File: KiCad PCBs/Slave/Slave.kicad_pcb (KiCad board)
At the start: 2 copper layers, 51 parts, among them J1 Screw_Terminal_01x02, J10 AVR-ISP-6, J11 Conn_01x06_Female, J12 Screw_Terminal_01x02, J13 Screw_Terminal_01x02, J14 Screw_Terminal_01x02, J15 Screw_Terminal_01x02, J16 Screw_Terminal_01x02, J2 Screw_Terminal_01x02, J3 Screw_Terminal_01x02, J4 Screw_Terminal_01x02, J5 Screw_Terminal_01x02, J6 Screw_Terminal_01x02, J7 Screw_Terminal_01x02, J8 Screw_Terminal_01x02, J9 Screw_Terminal_01x02, SW1 SW_DIP_x02, SW1 SW_DIP_x04, SW2 SW_DIP_x02, SW3 SW_MEC_5E, U1 ATmega328P-AU, U2 MAX487ESA+T, U3 ULN2003A, U4 LM358DR2G, U5 AMS1117-5.0, Y1 Crystal_GND24

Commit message: Slave PCB wip
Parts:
- removed the SW1 at (59.7, 137.7)
- moved C9 132.2 mm to (148.9, 110.5), turned to -45 degrees
- moved C8 123.1 mm to (147.0, 108.7), turned to -45 degrees
- moved Y1 104.6 mm to (145.9, 111.0), turned to -45 degrees
- moved C6 98.1 mm to (137.6, 99.7), turned to 180 degrees
- moved J11 91.7 mm to (121.3, 125.1)
- moved U3 75.6 mm to (121.3, 95.9), turned to 90 degrees
- moved RJ1 70.0 mm to (106.0, 110.5), turned to -90 degrees
- moved U2 47.7 mm to (140.8, 95.9), turned to 90 degrees
- moved J10 36.1 mm to (110.5, 128.9)
- moved U5 31.0 mm to (121.3, 108.6)
- moved U4 30.6 mm to (121.3, 116.8), turned to 90 degrees
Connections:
- C10 pad 1: VCC -> +12V
- U5 pad 3: VCC -> +12V
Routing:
- net +5V: track 11.6 -> 23.2 mm
- net TXD: track 0.00 -> 11.5 mm
- net XTAL1: track 0.00 -> 9.23 mm
- net XTAL2: track 0.00 -> 9.05 mm
- net D2: track 0.00 -> 6.79 mm, vias 0 -> 2
- net RXD: track 0.00 -> 5.72 mm

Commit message: Slave WIP
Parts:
- removed R5: 1K, Resistor_SMD:R_0402_1005Metric
- moved J7 151.2 mm to (162.9, 80.0), turned to -90 degrees
- moved D1 147.6 mm to (172.1, 118.1), turned to 90 degrees
- moved D2 146.0 mm to (165.1, 108.6)
- moved J8 130.1 mm to (152.9, 80.0), turned to -90 degrees
- moved R4 116.7 mm to (145.9, 88.3)
- moved SW3 113.9 mm to (165.1, 104.1)
- moved R2 112.4 mm to (167.6, 108.6), turned to 180 degrees
- moved J4 111.4 mm to (149.5, 128.3), turned to 90 degrees
- moved J9 110.0 mm to (142.9, 80.0), turned to -90 degrees
- moved C7 106.8 mm to (143.5, 94.0), turned to 90 degrees
- moved J16 100.7 mm to (130.8, 80.0), turned to -90 degrees
- moved J14 97.0 mm to (106.7, 80.0), turned to -90 degrees
- moved D5 96.1 mm to (145.4, 97.2)
- moved J5 95.7 mm to (159.5, 128.3), turned to 90 degrees
- moved J15 95.3 mm to (118.7, 80.0), turned to -90 degrees
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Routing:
- net +5V: track 23.2 -> 29.5 mm

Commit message: Slave WIP
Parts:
- removed D3, D4: D, A10 KiCad Libraries:SOD-123F_L2.8-W1.8-LS3.7-RD
- removed U4: LM358DR2G, Package_SO:SOIC-8_3.9x4.9mm_P1.27mm
- added R10: 1.8K, Resistor_SMD:R_0805_2012Metric, F.Cu at (121.3, 101.6)
- added R9: 1.8K, Resistor_SMD:R_0805_2012Metric, F.Cu at (121.3, 106.7)
- R7, R8: value 1K -> 1.8K; footprint Resistor_SMD:R_0402_1005Metric -> Resistor_SMD:R_0805_2012Metric
- moved C11 126.9 mm to (127.0, 87.6)
- moved C10 121.6 mm to (121.2, 96.5)
- moved R8 108.6 mm to (116.2, 87.0)
- moved R7 89.1 mm to (121.3, 104.1)
- moved J7 6.95 mm to (169.8, 80.0)
- moved J8 6.95 mm to (159.8, 80.0)
- moved J9 6.95 mm to (149.8, 80.0)
- moved U3 5.99 mm to (119.4, 115.6)
- moved SW1 0.90 mm to (130.8, 98.4)
- moved R6 0.81 mm to (127.6, 97.9)
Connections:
- R7 pad 2: +5V -> RXD
- R8 pad 2: ACT -> TXD
- RJ1 pad 1: +5V -> Net-(R9-Pad1)
- RJ1 pad 2: ACT -> Net-(R10-Pad1)
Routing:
- net +12V: track 0.00 -> 78.0 mm
- net RS485+: track 0.00 -> 35.3 mm
- net RS485-: track 0.00 -> 34.2 mm, vias 0 -> 2
- net +5V: track 29.5 -> 47.6 mm
- net Net-(R9-Pad1): track 0.00 -> 13.6 mm, vias 0 -> 2
- net Net-(R10-Pad1): track 0.00 -> 10.1 mm, vias 0 -> 2
- net RS485_GND: track 0.00 -> 8.71 mm
- net Net-(R6-Pad2): track 0.00 -> 5.71 mm
- net Net-(R7-Pad1): track 0.00 -> 5.49 mm
- net Net-(R8-Pad1): track 0.00 -> 4.70 mm
- net RXD: track 5.72 -> 8.26 mm
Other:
- board outline added: 83.8 x 71.1 mm
- board text added: "1 BCK LT"
- board text added: "1 RS485"
- board text added: "2 AUX LT"
- board text added: "2 TERM"

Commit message: Slave WIP
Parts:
- C8, C9: value 16pF -> 15pF
- R1, R2, R3, R4, R6: footprint Resistor_SMD:R_0402_1005Metric -> Resistor_SMD:R_0805_2012Metric
- moved J10 14.6 mm to (166.4, 105.4)
- moved R4 12.4 mm to (134.0, 91.4), turned to 180 degrees
- moved J13 12.1 mm to (105.4, 115.6)
- moved J12 11.4 mm to (105.4, 127.0)
- moved R2 10.0 mm to (164.6, 99.1), turned to 0 degrees
- moved SW3 9.86 mm to (167.6, 94.6)
- moved D2 9.86 mm to (167.6, 99.1), turned to 180 degrees
- moved J11 8.25 mm to (137.2, 91.4)
- moved SW2 4.66 mm to (134.6, 115.1)
- moved C7 1.91 mm to (145.4, 94.0), turned to 180 degrees
- moved C11 1.42 mm to (127.6, 86.4), turned to 90 degrees
- moved R8 1.35 mm to (115.3, 88.0), turned to 90 degrees
- moved R6 1.30 mm to (126.5, 97.3)
- moved D5 1.27 mm to (145.4, 95.9)
- moved U3 0.90 mm to (118.7, 114.9)
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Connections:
- J1 pad 1: D2 -> GND
- R1 pad 1: D13/SCK -> D13
- SW2 pad 1: D3 -> D5
- SW2 pad 2: D4 -> D6
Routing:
- net RESET: track 0.00 -> 55.5 mm, vias 0 -> 2
- net D13: track 0.00 -> 51.2 mm
- net TXD: track 11.5 -> 57.1 mm, vias 0 -> 6
- net D5: track 0.00 -> 43.1 mm
- net D6: track 0.00 -> 41.9 mm, vias 0 -> 2
- net D3: track 0.00 -> 38.4 mm, vias 0 -> 2
- net D12: track 0.00 -> 37.2 mm, vias 0 -> 2
- net D11: track 0.00 -> 36.8 mm, vias 0 -> 2
- net +5V: track 47.6 -> 83.8 mm, vias 0 -> 3
- net D4: track 0.00 -> 33.8 mm, vias 0 -> 2
- net D7: track 0.00 -> 32.7 mm
- net RXD: track 8.26 -> 40.6 mm, vias 0 -> 5
- net A0: track 0.00 -> 32.1 mm
- net A5: track 0.00 -> 31.0 mm
- net D8: track 0.00 -> 29.3 mm
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- added copper zone on F.Cu, net +5V
- added copper zone on B.Cu, net GND
- added copper zone on F.Cu, net GND
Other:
- board size 83.8 x 71.1 mm -> 73 x 55.9 mm
- board text added: "GND"
- board text added: "INPUT ← D5 → BACKLIGHT"
- board text added: "INPUT ← D6 → AUX LIGHT"
- board text added: "OFF ← RS485 → ON"
- board text added: "OFF ← TERM → ON"
- board text added: "WarthogAtHome.com"
- board text removed: "1 BCK LT"
- board text removed: "1 RS485"
- board text removed: "2 AUX LT"
- board text removed: "2 TERM"

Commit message: Generated Final Rev 1 files for Hub and Slave
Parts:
- removed R10, R9: 1.8K, Resistor_SMD:R_0805_2012Metric
- moved R8 17.2 mm to (121.3, 104.1), turned to 0 degrees
- moved R7 2.54 mm to (121.3, 101.6)
- moved J10 0.89 mm to (165.5, 105.4)
- moved R2 0.25 mm to (164.3, 99.1)
- moved U5 0.25 mm to (123.8, 91.8)
- moved R1 0.25 mm to (172.1, 114.8)
- moved SW2 0.13 mm to (134.5, 115.1)
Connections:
- RJ1 pad 1: Net-(R9-Pad1) -> TXD
- RJ1 pad 2: Net-(R10-Pad1) -> RXD
- SW3 pad 1: unconnected-(SW3-Pad1) -> GND
- SW3 pad 4: unconnected-(SW3-Pad4) -> RESET
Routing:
- net Net-(R8-Pad1): track 2.77 -> 16.5 mm, vias 0 -> 2
- net Net-(R9-Pad1): track 13.6 -> 0.00 mm, vias 2 -> 0
- net RXD: track 40.6 -> 52.6 mm, vias 5 -> 6
- net Net-(R10-Pad1): track 10.1 -> 0.00 mm, vias 2 -> 0
- net RESET: track 55.5 -> 57.8 mm
- net TXD: track 57.1 -> 55.7 mm
- net D12: track 37.2 -> 36.3 mm
- net D11: track 36.8 -> 35.9 mm
- net +5V: track 83.8 -> 83.1 mm
- net D13: track 51.2 -> 50.6 mm
- net GND: track 7.11 -> 7.21 mm, vias 33 -> 38
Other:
- board text added: "BRRRRRRRRT"
- board text removed: "GND"

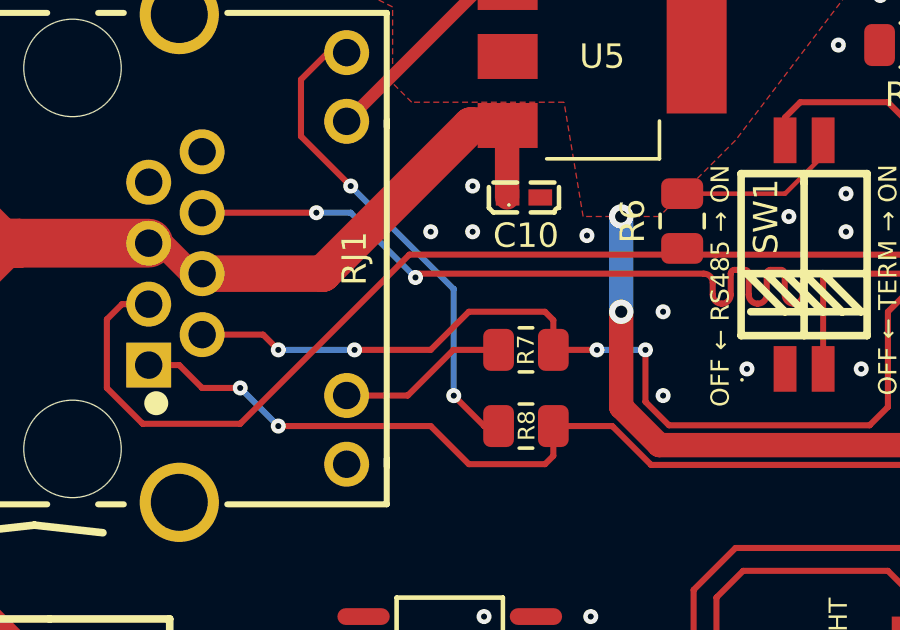
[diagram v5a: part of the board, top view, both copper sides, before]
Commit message: Fixed swapped LEDs on Slave
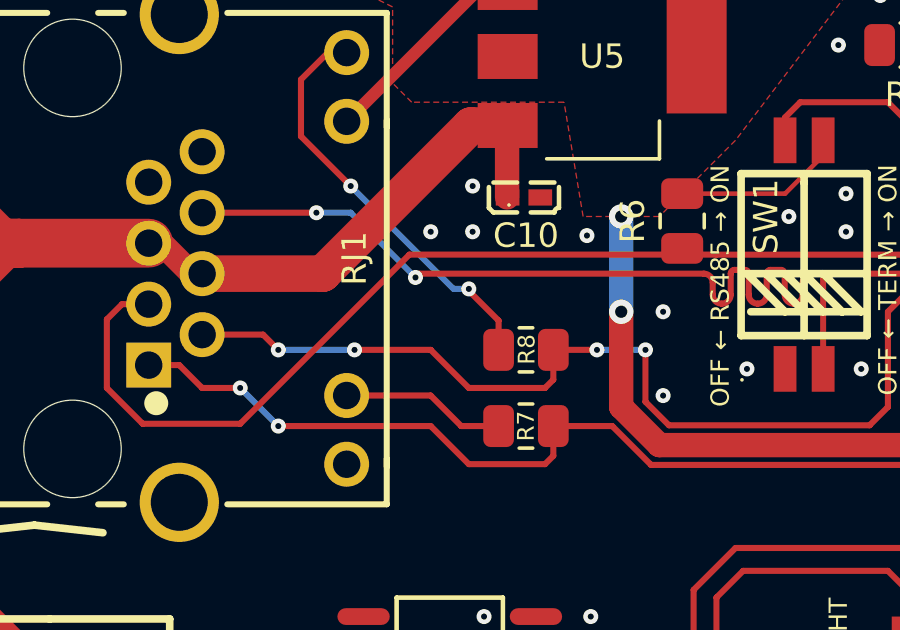
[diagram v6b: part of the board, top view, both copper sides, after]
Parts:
- moved R7 2.54 mm to (121.3, 104.1)
- moved R8 2.54 mm to (121.3, 101.6)
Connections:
- R7 pad 2: RXD -> TXD
- R8 pad 2: TXD -> RXD
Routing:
- net Net-(R8-Pad1): track 16.5 -> 13.9 mm
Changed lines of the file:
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@@
   (net 45 "GND")
   (footprint "Resistor_SMD:R_0805_2012Metric" (layer "F.Cu")
-    (at 121.285 101.6)
+    (at 121.285 104.14)
     (descr "Resistor SMD 0805 (2012 Metric), square (rectangular) end terminal, IPC_7351 nominal, (Body size source: IPC-SM-782 page 72, https://www.pcb-3d.com/wordpress/wp-content/uploads/ipc-sm-782a_amendment_1_and_2.pdf), generated with kicad-footprint-generator")
     (tags "resistor")
@@
       (net 31 "Net-(R7-Pad1)") (pintype "passive"))
     (pad "2" smd roundrect (at 0.9125 0) (size 1.025 1.4) (layers "F.Cu" "F.Paste" "F.Mask") (roundrect_rratio 0.243902439)
-      (net 28 "RXD") (pintype "passive"))
+      (net 27 "TXD") (pintype "passive"))
     (model "${KICAD6_3DMODEL_DIR}/Resistor_SMD.3dshapes/R_0805_2012Metric.wrl"
       (offset (xyz 0 0 0))
@@
   )
   (footprint "Resistor_SMD:R_0805_2012Metric" (layer "F.Cu")
-    (at 121.285 104.14)
+    (at 121.285 101.6)
     (descr "Resistor SMD 0805 (2012 Metric), square (rectangular) end terminal, IPC_7351 nominal, (Body size source: IPC-SM-782 page 72, https://www.pcb-3d.com/wordpress/wp-content/uploads/ipc-sm-782a_amendment_1_and_2.pdf), generated with kicad-footprint-generator")
     (tags "resistor")
@@
       (net 32 "Net-(R8-Pad1)") (pintype "passive"))
     (pad "2" smd roundrect (at 0.9125 0) (size 1.025 1.4) (layers "F.Cu" "F.Paste" "F.Mask") (roundrect_rratio 0.243902439)
-      (net 27 "TXD") (pintype "passive"))
+      (net 28 "RXD") (pintype "passive"))
     (model "${KICAD6_3DMODEL_DIR}/Resistor_SMD.3dshapes/R_0805_2012Metric.wrl"
       (offset (xyz 0 0 0))
@@
   (segment (start 155.575 85.09) (end 152.4 81.915) (width 0.2032) (layer "F.Cu") (net 26))
   (segment (start 147.02853 80.98853) (end 147.02853 80.01) (width 0.2032) (layer "F.Cu") (net 26))
-  (segment (start 124.161054 104.14) (end 122.1975 104.14) (width 0.2032) (layer "F.Cu") (net 27))
   (segment (start 111.76 102.87) (end 110.49 102.87) (width 0.2032) (layer "F.Cu") (net 27))
   (segment (start 118.11 104.14) (end 119.38 105.41) (width 0.2032) (layer "F.Cu") (net 27))
@@
   (segment (start 121.92 105.41) (end 122.1975 105.1325) (width 0.2032) (layer "F.Cu") (net 27))
   (segment (start 113.03 104.14) (end 118.11 104.14) (width 0.2032) (layer "F.Cu") (net 27))
+  (segment (start 124.161054 104.14) (end 122.1975 104.14) (width 0.2032) (layer "F.Cu") (net 27))
   (segment (start 139.7 95.25) (end 139.7 92.075) (width 0.2032) (layer "F.Cu") (net 27))
   (segment (start 137.16 104.14) (end 135.8646 105.4354) (width 0.2032) (layer "F.Cu") (net 27))
@@
   (segment (start 113.03 104.14) (end 111.76 102.87) (width 0.2032) (layer "B.Cu") (net 27))
   (segment (start 142.259005 97.174005) (end 142.24 97.155) (width 0.2032) (layer "B.Cu") (net 27))
-  (segment (start 118.11 101.6) (end 119.38 100.33) (width 0.2032) (layer "F.Cu") (net 28))
   (segment (start 144.352947 100.330003) (end 142.874997 100.330003) (width 0.2032) (layer "F.Cu") (net 28))
   (segment (start 142.24 92.075) (end 142.265 92.05) (width 0.1524) (layer "F.Cu") (net 28))
   (segment (start 133.35 103.505) (end 132.7404 104.1146) (width 0.2032) (layer "F.Cu") (net 28))
   (segment (start 142.875 93.345) (end 142.24 92.71) (width 0.2032) (layer "F.Cu") (net 28))
-  (segment (start 122.1975 101.6) (end 122.1975 100.6075) (width 0.2032) (layer "F.Cu") (net 28))
+  (segment (start 121.92 102.87) (end 122.1975 102.5925) (width 0.2032) (layer "F.Cu") (net 28))
   (segment (start 146.006268 101.983324) (end 144.352947 100.330003) (width 0.2032) (layer "F.Cu") (net 28))
   (segment (start 125.2683 103.3317) (end 125.2683 101.6) (width 0.2032) (layer "F.Cu") (net 28))
+  (segment (start 122.1975 102.5925) (end 122.1975 101.6) (width 0.2032) (layer "F.Cu") (net 28))
   (segment (start 133.35 100.33) (end 133.35 103.505) (width 0.2032) (layer "F.Cu") (net 28))
-  (segment (start 115.57 101.6) (end 118.11 101.6) (width 0.2032) (layer "F.Cu") (net 28))
-  (segment (start 123.6517 101.6) (end 122.1975 101.6) (width 0.2032) (layer "F.Cu") (net 28))
-  (segment (start 122.1975 100.6075) (end 121.92 100.33) (width 0.2032) (layer "F.Cu") (net 28))
+  (segment (start 119.38 102.87) (end 121.92 102.87) (width 0.2032) (layer "F.Cu") (net 28))
+  (segment (start 118.11 101.6) (end 119.38 102.87) (width 0.2032) (layer "F.Cu") (net 28))
   (segment (start 142.874997 100.330003) (end 140.969999 100.330003) (width 0.2032) (layer "F.Cu") (net 28))
   (segment (start 126.0512 104.1146) (end 125.2683 103.3317) (width 0.2032) (layer "F.Cu") (net 28))
@@
   (segment (start 112.522004 101.092004) (end 110.49 101.092004) (width 0.2032) (layer "F.Cu") (net 28))
   (segment (start 137.160003 100.330003) (end 136.525 99.695) (width 0.2032) (layer "F.Cu") (net 28))
-  (segment (start 119.38 100.33) (end 121.92 100.33) (width 0.2032) (layer "F.Cu") (net 28))
   (segment (start 136.525 99.695) (end 133.985 99.695) (width 0.2032) (layer "F.Cu") (net 28))
   (segment (start 140.969999 100.330003) (end 137.160003 100.330003) (width 0.2032) (layer "F.Cu") (net 28))
   (segment (start 142.24 92.71) (end 142.24 92.075) (width 0.2032) (layer "F.Cu") (net 28))
+  (segment (start 123.6517 101.6) (end 122.1975 101.6) (width 0.2032) (layer "F.Cu") (net 28))
   (segment (start 142.874997 100.330003) (end 142.875 100.33) (width 0.1524) (layer "F.Cu") (net 28))
   (segment (start 142.875 98.425) (end 142.875 93.345) (width 0.2032) (layer "F.Cu") (net 28))
+  (segment (start 115.57 101.6) (end 118.11 101.6) (width 0.2032) (layer "F.Cu") (net 28))
   (via (at 142.875 98.425) (size 0.5) (drill 0.2) (layers "F.Cu" "B.Cu") (net 28))
   (via (at 113.03 101.6) (size 0.5) (drill 0.2) (layers "F.Cu" "B.Cu") (net 28))
@@
   (segment (start 131.191001 95.122999) (end 129.921 96.393) (width 0.1524) (layer "F.Cu") (net 30))
   (segment (start 131.191001 94.614992) (end 131.191001 95.122999) (width 0.1524) (layer "F.Cu") (net 30))
-  (segment (start 118.866936 101.6) (end 117.345468 103.121468) (width 0.2032) (layer "F.Cu") (net 31))
-  (segment (start 117.345468 103.121468) (end 115.308389 103.121468) (width 0.2032) (layer "F.Cu") (net 31))
-  (segment (start 120.3725 101.6) (end 118.866936 101.6) (width 0.2032) (layer "F.Cu") (net 31))
-  (segment (start 119.891856 104.14) (end 118.877459 103.125603) (width 0.2032) (layer "F.Cu") (net 32))
+  (segment (start 119.126 104.14) (end 118.107468 103.121468) (width 0.2032) (layer "F.Cu") (net 31))
+  (segment (start 120.3725 104.14) (end 119.126 104.14) (width 0.2032) (layer "F.Cu") (net 31))
+  (segment (start 118.107468 103.121468) (end 115.308389 103.121468) (width 0.2032) (layer "F.Cu") (net 31))
+  (segment (start 119.38 99.568) (end 119.38 99.6315) (width 0.2032) (layer "F.Cu") (net 32))
+  (segment (start 120.3725 100.624) (end 120.3725 101.6) (width 0.2032) (layer "F.Cu") (net 32))
+  (segment (start 119.38 99.6315) (end 120.3725 100.624) (width 0.2032) (layer "F.Cu") (net 32))
   (segment (start 113.785672 94.481672) (end 113.785672 92.589328) (width 0.2032) (layer "F.Cu") (net 32))
   (segment (start 113.792 94.488) (end 113.785672 94.481672) (width 0.2032) (layer "F.Cu") (net 32))
-  (segment (start 120.3725 104.14) (end 119.891856 104.14) (width 0.2032) (layer "F.Cu") (net 32))
   (segment (start 114.683555 91.691445) (end 113.785672 92.589328) (width 0.2032) (layer "F.Cu") (net 32))
   (segment (start 115.308389 91.691445) (end 114.683555 91.691445) (width 0.2032) (layer "F.Cu") (net 32))
   (segment (start 115.443 96.139) (end 113.792 94.488) (width 0.2032) (layer "F.Cu") (net 32))
   (via (at 115.443 96.139) (size 0.5) (drill 0.2) (layers "F.Cu" "B.Cu") (free) (net 32))
-  (via (at 118.877459 103.125603) (size 0.5) (drill 0.2) (layers "F.Cu" "B.Cu") (net 32))
-  (segment (start 115.443 96.139) (end 118.877459 99.573459) (width 0.2032) (layer "B.Cu") (net 32))
-  (segment (start 118.877459 99.573459) (end 118.877459 103.125603) (width 0.2032) (layer "B.Cu") (net 32))
+  (via (at 119.38 99.568) (size 0.5) (drill 0.2) (layers "F.Cu" "B.Cu") (net 32))
+  (segment (start 118.872 99.568) (end 115.443 96.139) (width 0.2032) (layer "B.Cu") (net 32))
+  (segment (start 119.38 99.568) (end 118.872 99.568) (width 0.2032) (layer "B.Cu") (net 32))
   (segment (start 102.87 97.155) (end 102.87 81.31873) (width 1.6256) (layer "F.Cu") (net 33))
   (segment (start 102.87 121.92) (end 105.41 124.46) (width 1.6256) (layer "F.Cu") (net 33))
